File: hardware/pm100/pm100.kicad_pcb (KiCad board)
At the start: 2 copper layers, 46.2 x 68.6 mm, 75 parts, among them J1 VCC-BATT, J10 NRST, J11 Display, J12 USART2-TX, J13 USART2-RX, J14 BOOT0, J15 GND, J16 3V3, J17 3V3, J2 VCC-ESC, J3 USB_B_Micro, J4 GND-BATT, J5 UART, J6 RECEIVER, J7 ESC, J8 SWDIO, J9 SWCLK, Q5 BSS138, Q6 BSS138, Q7 BSS138, Q8 BSS138, SW1 CLASSE, SW2 Boot0, SW3 Reset, U2 STM32L052C6Tx, U3 LD1117S50TR_SOT223, U5 LD1117S33TR_SOT223, U7 TPS2113A, U8 INA226, Y1 32.768khz, Y3 8mhz

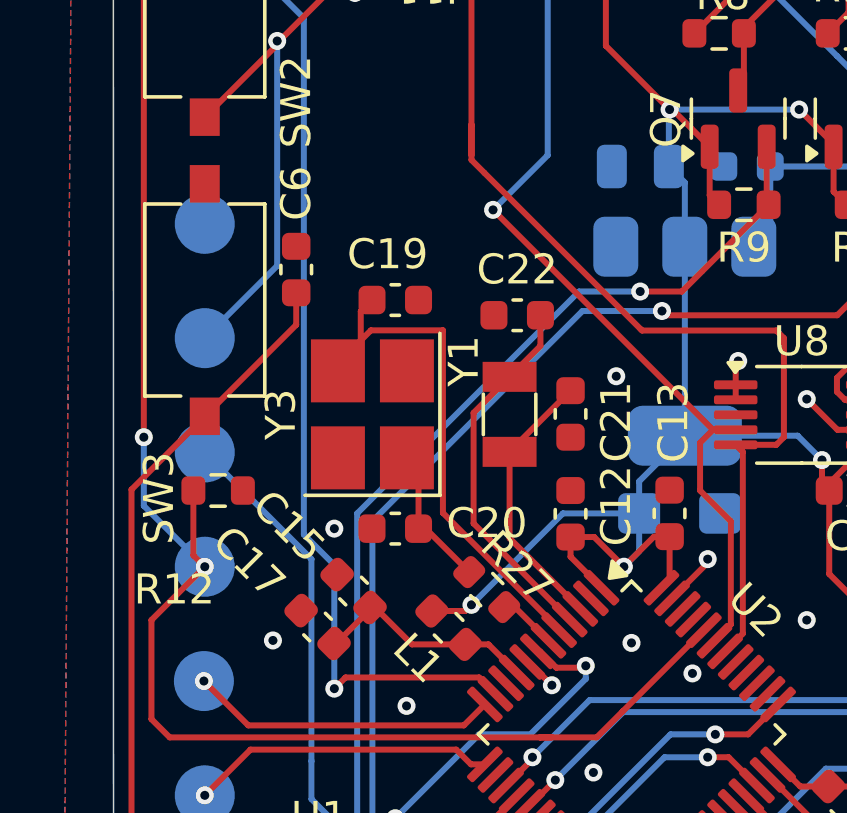
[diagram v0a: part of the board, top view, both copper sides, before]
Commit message: adicionado GND no cristal de 8mhz
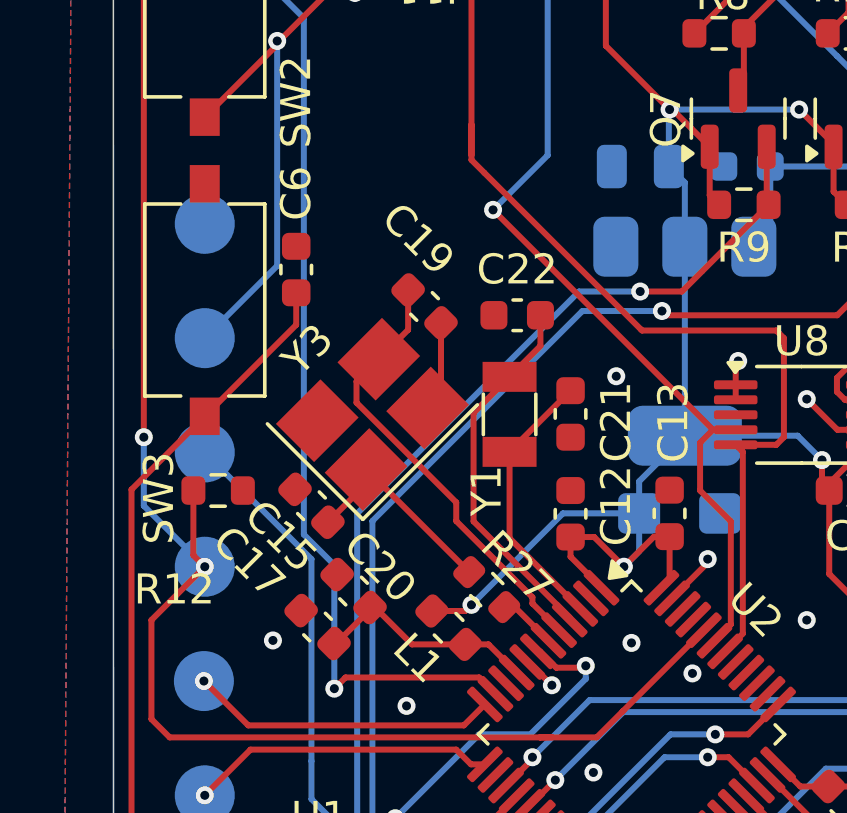
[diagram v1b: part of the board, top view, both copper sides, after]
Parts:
- moved C20 2.90 mm to (133.1, 70.4), turned to -45 degrees
- moved C19 1.00 mm to (136.9, 63.7), turned to -45 degrees
- turned Y3 to 45 degrees
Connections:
- Y3 pad 2: unconnected-(Y3-Pad2) -> GND
- Y3 pad 4: unconnected-(Y3-Pad4) -> GND
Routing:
- net Net-(U2-PH0): track 18.3 -> 14.8 mm
- net GND: track 45.0 -> 48.0 mm, vias 26 -> 25
- net Net-(C20-Pad2): track 4.81 -> 7.14 mm

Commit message: usando Xiao Ble
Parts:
- moved R27 2.96 mm to (136.4, 71.6), turned to 45 degrees
- moved Y1 2.19 mm to (140.1, 69.5), turned to -45 degrees
- moved C22 2.01 mm to (140.6, 65.9), turned to 90 degrees
- moved C12 1.52 mm to (143.3, 70.6)
- moved C21 0.57 mm to (142.2, 67.6), turned to -90 degrees
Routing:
- net GND: track 48.0 -> 59.9 mm, vias 25 -> 14
- net PWM-INPUT: track 33.4 -> 38.0 mm
- net PWM-OUTPUT: track 60.3 -> 64.0 mm
- net Net-(U2-PH1): track 1.94 -> 5.63 mm
- net USB_DP: track 15.3 -> 18.6 mm
- net Net-(U2-PC15): track 12.4 -> 9.08 mm
- net Net-(J5-Pin_2): track 16.0 -> 12.9 mm, vias 0 -> 1
- net SLAVE_SDA: track 45.0 -> 42.2 mm
- net USB_DM: track 16.1 -> 19.0 mm
- net +5V: track 76.3 -> 79.1 mm
- net +3V3: track 156.7 -> 159.3 mm
- net Net-(J9-Pin_1): track 23.5 -> 25.8 mm
- net Net-(U2-PC14): track 9.09 -> 6.87 mm
- net Net-(C20-Pad2): track 7.14 -> 5.01 mm
- net I2C-SCL: track 34.0 -> 32.7 mm
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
